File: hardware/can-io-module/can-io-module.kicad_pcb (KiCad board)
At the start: 2 copper layers, 96 x 86 mm, 79 parts, among them J1 ECU_FCI_24P_RightAngle, Q1 60V P-channel reverse polarity, Q4 60V logic N-MOS RELAY1, Q5 60V logic N-MOS RELAY2, U1 STM32G0B1CBT6, U10 MAX31855KASA+, U11 Schmitt Flex front end, U2 LMR16006Y-Q1, U3 3V3 LDO 300mA, U4 SENSOR_5V load switch, U5 74HCT4051 1K excitation, U6 74HCT4051 4K7 excitation, U7 L9613, U8 TJA1051T/3, U9 TLV9002-Q1

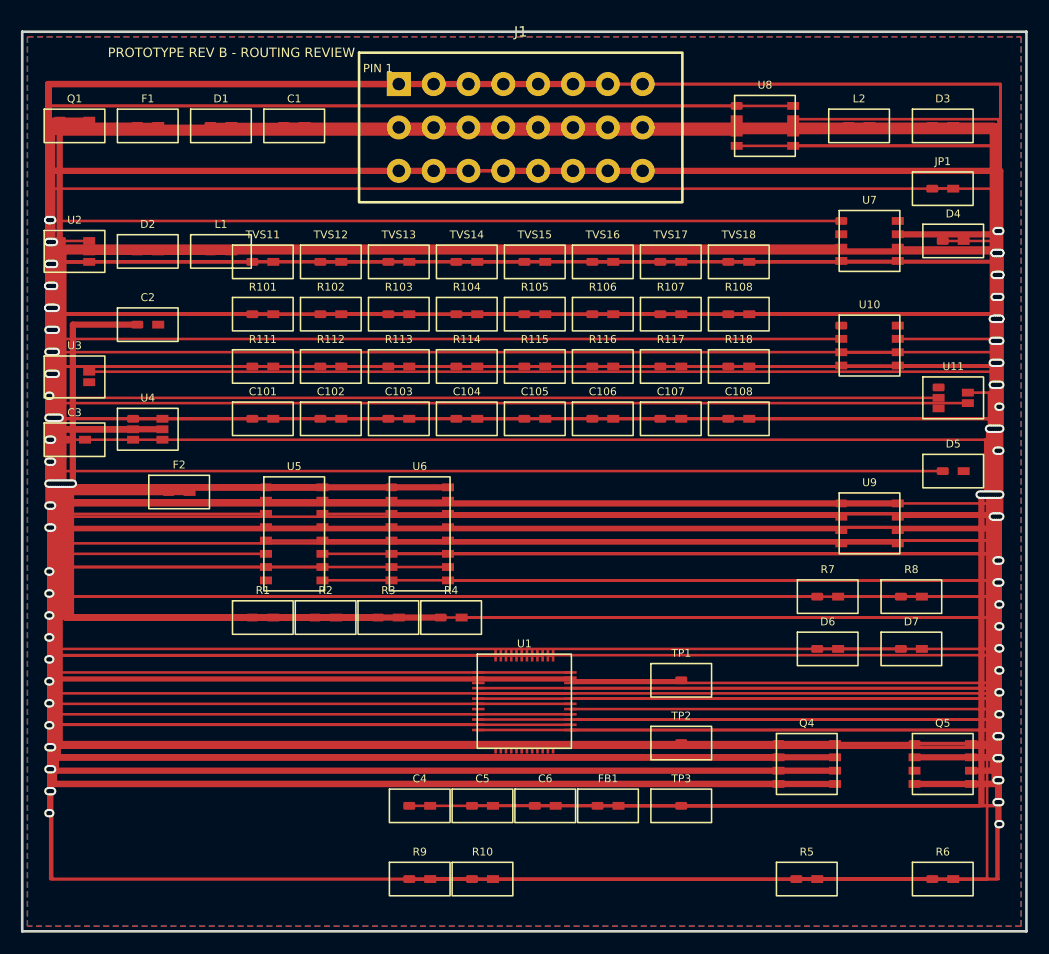
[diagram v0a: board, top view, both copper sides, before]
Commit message: feat: check in verified two-layer CAN IO route
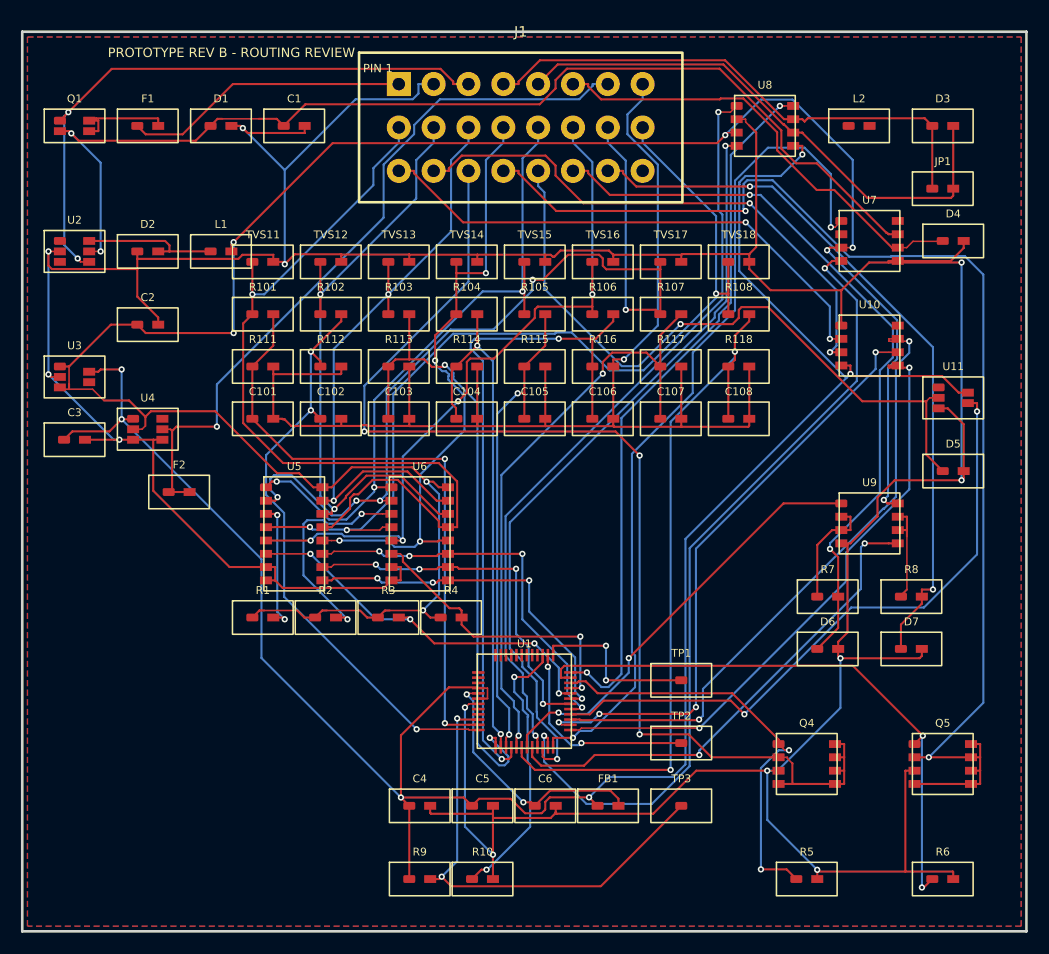
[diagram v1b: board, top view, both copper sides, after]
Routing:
- net +3V3: track 843.1 -> 209.9 mm, vias 12 -> 6
- net RELAY_OUT1: track 704.0 -> 113.5 mm, vias 7 -> 3
- net POWER_GND: track 0.00 -> 415.8 mm, vias 0 -> 12
- net +5V: track 610.4 -> 216.9 mm, vias 14 -> 8
- net VBAT_PROTECTED: track 494.7 -> 105.5 mm, vias 5 -> 2
- net AOUT1_OP: track 319.1 -> 10.9 mm, vias 3 -> 0
- net AIN2: track 363.2 -> 61.8 mm, vias 5 -> 2
- net CAN_L: track 341.2 -> 52.5 mm, vias 4 -> 0
- net AIN4: track 337.8 -> 60.7 mm, vias 5 -> 4
- net ADC_IN2: track 321.1 -> 57.6 mm, vias 4 -> 3
- net AIN6: track 318.0 -> 70.7 mm, vias 5 -> 4
- net ADC_IN4: track 273.1 -> 50.5 mm, vias 4 -> 2
- net ADC_IN7: track 281.1 -> 58.9 mm, vias 4 -> 2
- net AOUT2: track 277.1 -> 68.9 mm, vias 3 -> 2
- net ADC_IN5: track 249.4 -> 46.7 mm, vias 4 -> 2
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
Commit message: feat: generate connected CAN IO schematic and SWD header
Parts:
- added J2: SWD_1x05_P2.54mm_DNP, Connector_PinHeader_2.54mm:PinHeader_1x05_P2.54mm_Vertical, F.Cu at (86.0, 92.0)
- U4: footprint DIY_DASH:SC70-6 -> DIY_DASH:SC70-5
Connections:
- F2 pad 1: SENSOR_5V -> SENSOR_5V_SW
- L2 pad 1: (no net) -> CAN_H_PROTECTED
- L2 pad 2: (no net) -> CAN_L_PROTECTED
- U1 pad 15: ADC_IN5 -> DAC1_RAW
- U1 pad 16: ADC_IN6 -> DAC2_RAW
- U1 pad 17: ADC_IN7 -> ADC_IN5
- U1 pad 18: ADC_IN8 -> ADC_IN6
- U1 pad 19: DAC1_RAW -> ADC_IN7
- U1 pad 20: DAC2_RAW -> ADC_IN8
- U1 pad 21: CAN_TX -> BOOT0
- U1 pad 22: CAN_RX -> VBAT_MON
- U1 pad 23: KTX -> V5_MON
- U1 pad 24: KRX -> V3V3_MON
- U1 pad 25: EGT_SCK -> RELAY2_GATE
- U1 pad 26: EGT_CS -> CAN_SILENT
- U1 pad 27: EGT_SO -> SENSOR_5V_EN
- U1 pad 29: PULL_A0 -> IGN_SENSE
- U1 pad 30: PULL_A1 -> PULL_4K7_EN_N
- U1 pad 31: PULL_A2 -> RELAY1_GATE
- U1 pad 32: PULL_1K_EN_N -> SERVICE
- U1 pad 33: PULL_4K7_EN_N -> CAN_RX
- U1 pad 34: RELAY1_GATE -> CAN_TX
- U1 pad 35: RELAY2_GATE -> SWDIO
- U1 pad 36: CAN_SILENT -> SWCLK
- U1 pad 37: SWDIO -> KLINE_ENABLE
- U1 pad 38: SWCLK -> PULL_A0
- U1 pad 39: BOOT0 -> PULL_A1
- U1 pad 40: (no net) -> PULL_A2
- U1 pad 41: (no net) -> PULL_1K_EN_N
- U1 pad 42: (no net) -> EGT_SCK
- U1 pad 43: (no net) -> EGT_SO
- U1 pad 44: (no net) -> EGT_CS
- U1 pad 45: (no net) -> KTX
- U1 pad 46: (no net) -> KRX
- U4 pad 1: +3V3 -> SENSOR_5V_SW
- U4 pad 2: +5V -> POWER_GND
- U4 pad 3: POWER_GND -> SENSOR_5V_OC
- U4 pad 4: POWER_GND -> SENSOR_5V_EN
- U4 pad 5: SENSOR_5V -> +5V
- U8 pad 6: CAN_L -> CAN_L_PROTECTED
- U8 pad 7: CAN_H -> CAN_H_PROTECTED
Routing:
- net +3V3: track 209.9 -> 808.2 mm, vias 6 -> 12
- net RELAY_OUT1: track 113.5 -> 704.0 mm, vias 3 -> 7
- net POWER_GND: track 415.8 -> 0.00 mm, vias 12 -> 0
- net +5V: track 216.9 -> 613.7 mm, vias 8 -> 14
- net VBAT_PROTECTED: track 105.5 -> 494.7 mm, vias 2 -> 5
- net AOUT1_OP: track 10.9 -> 319.1 mm, vias 0 -> 3
- net AIN2: track 61.8 -> 363.2 mm, vias 2 -> 5
- net CAN_L: track 52.5 -> 350.0 mm, vias 0 -> 4
- net AIN4: track 60.7 -> 337.8 mm, vias 4 -> 5
- net AIN6: track 70.7 -> 318.0 mm, vias 4 -> 5
- net ADC_IN2: track 57.6 -> 288.4 mm, vias 3 -> 4
- net NRST: track 45.5 -> 260.6 mm, vias 2 -> 4
- net ADC_IN7: track 58.9 -> 269.7 mm, vias 2 -> 4
- net AOUT2: track 68.9 -> 277.1 mm, vias 2 -> 3
- net AIN7: track 87.6 -> 288.3 mm
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
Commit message: fix: make CAN IO symbol and footprint libraries self contained
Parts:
- J2: footprint Connector_PinHeader_2.54mm:PinHeader_1x05_P2.54mm_Vertical -> DIY_DASH:SWD_1x05_P2.54mm_Vertical
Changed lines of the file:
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@@
     (pad "24" thru_hole oval (at 23.31 8.30) (size 2.3 2.3) (drill 1.2) (layers "*.Cu" "*.Mask") (net 24 "SERVICE") (pinfunction "SERVICE") (pintype "passive"))
   )
-  (footprint "Connector_PinHeader_2.54mm:PinHeader_1x05_P2.54mm_Vertical" (layer "F.Cu")
+  (footprint "DIY_DASH:SWD_1x05_P2.54mm_Vertical" (layer "F.Cu")
     (at 86.0 92.0)
     (property "Reference" "J2" (at 0 -2.33) (layer "F.SilkS") (effects (font (size 0.8 0.8) (thickness 0.12))))

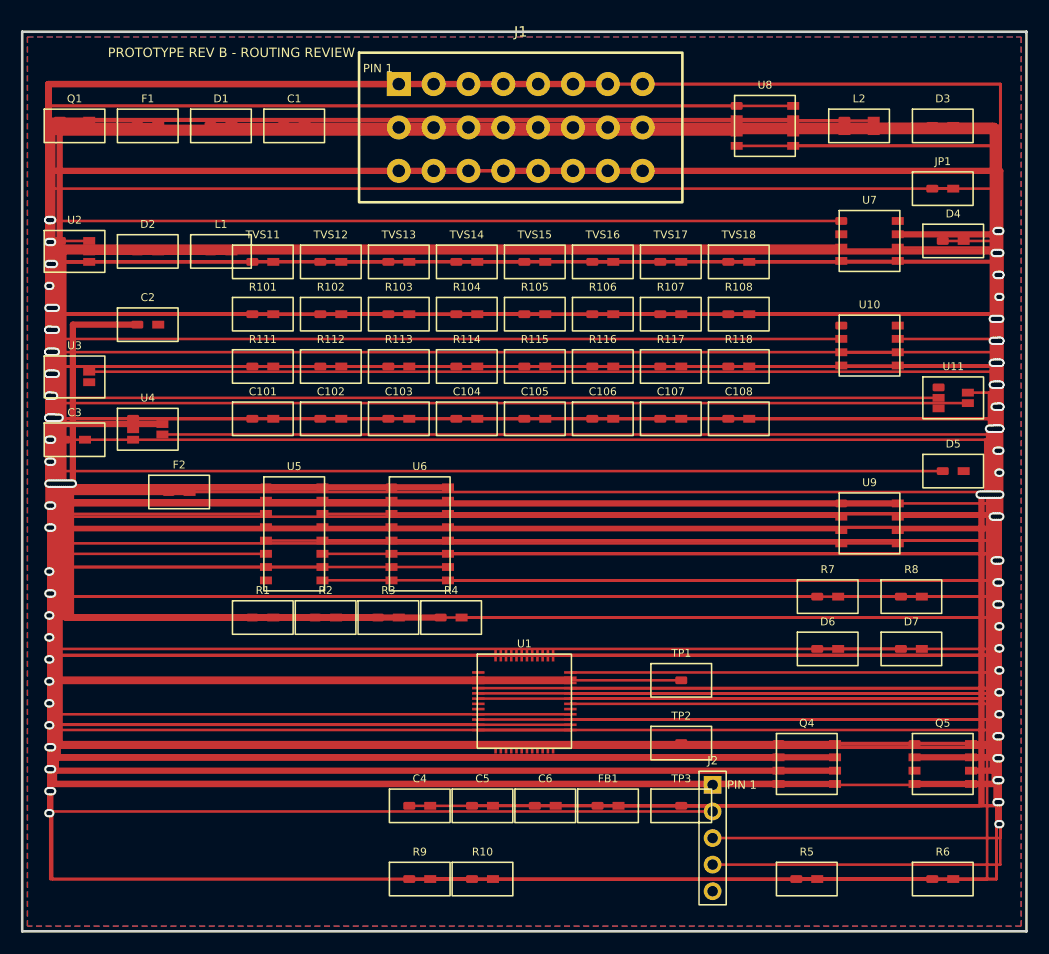
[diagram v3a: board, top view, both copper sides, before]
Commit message: fix: complete CAN IO power monitor support circuits
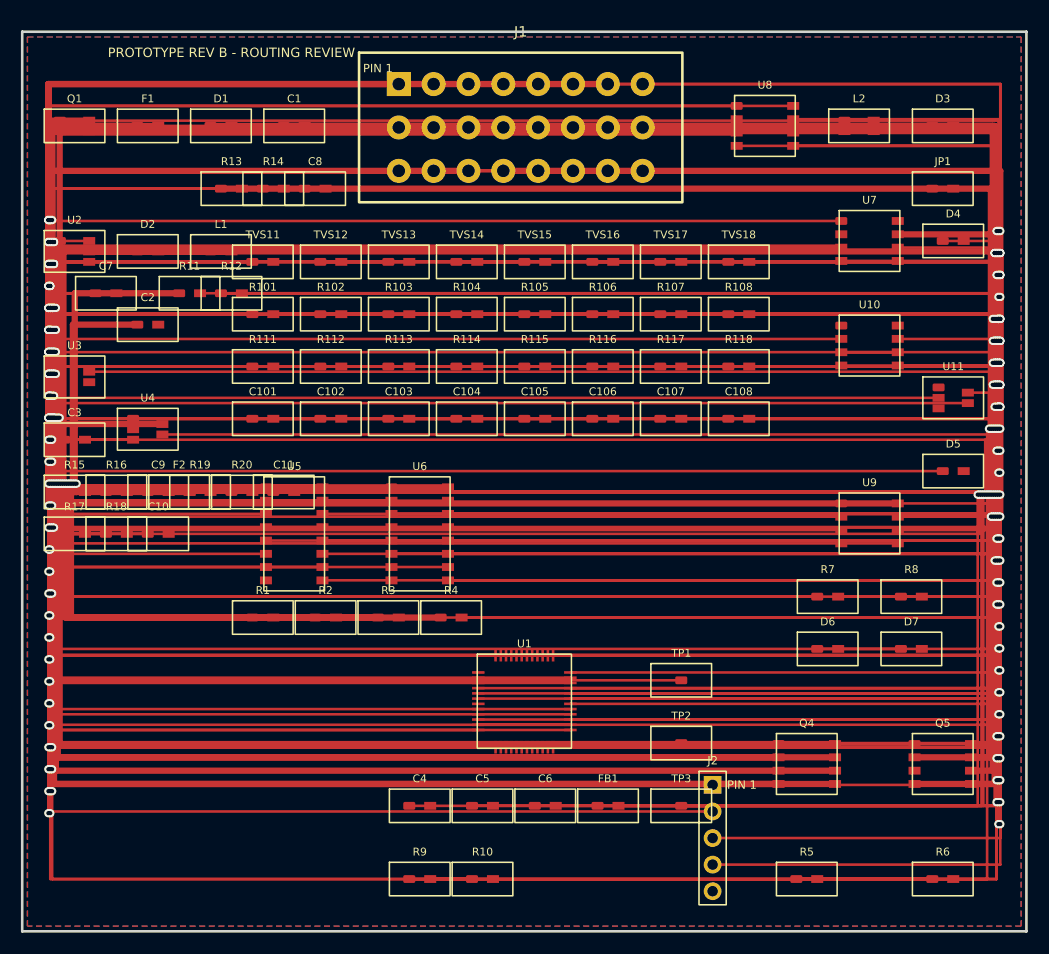
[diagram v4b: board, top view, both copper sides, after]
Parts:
- added C10: 10nF 3V3 monitor filter, DIY_DASH:0603, F.Cu at (33.0, 68.0)
- added C11: 10nF IGN sense filter, DIY_DASH:0603, F.Cu at (45.0, 64.0)
- added C7: 100nF buck bootstrap, DIY_DASH:0603, F.Cu at (28.0, 45.0)
- added C8: 10nF VBAT monitor filter, DIY_DASH:0603, F.Cu at (48.0, 35.0)
- added C9: 10nF 5V monitor filter, DIY_DASH:0603, F.Cu at (33.0, 64.0)
- added R11: 40.2k 1% buck FB upper, DIY_DASH:0603, F.Cu at (36.0, 45.0)
- added R12: 10.0k 1% buck FB lower, DIY_DASH:0603, F.Cu at (40.0, 45.0)
- added R13: 100k 1% VBAT monitor upper, DIY_DASH:0603, F.Cu at (40.0, 35.0)
- added R14: 15.0k 1% VBAT monitor lower, DIY_DASH:0603, F.Cu at (44.0, 35.0)
- added R15: 10.0k 1% 5V monitor upper, DIY_DASH:0603, F.Cu at (25.0, 64.0)
- added R16: 18.0k 1% 5V monitor lower, DIY_DASH:0603, F.Cu at (29.0, 64.0)
- added R17: 1.00k 1% 3V3 monitor upper, DIY_DASH:0603, F.Cu at (25.0, 68.0)
- added R18: 100k 1% 3V3 monitor lower, DIY_DASH:0603, F.Cu at (29.0, 68.0)
- added R19: 100k 1% IGN sense upper, DIY_DASH:0603, F.Cu at (37.0, 64.0)
- added R20: 15.0k 1% IGN sense lower, DIY_DASH:0603, F.Cu at (41.0, 64.0)
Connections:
- U1 pad 37: KLINE_ENABLE -> (no net)
- U1 pad 47: (no net) -> SENSOR_5V_OC
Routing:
- net V5_MON: track 0.00 -> 413.6 mm, vias 0 -> 4
- net BUCK_FB: track 0.00 -> 314.2 mm, vias 0 -> 3
- net IGN_SENSE: track 0.00 -> 195.6 mm, vias 0 -> 4
- net V3V3_MON: track 0.00 -> 190.3 mm, vias 0 -> 4
- net VBAT_MON: track 0.00 -> 174.4 mm, vias 0 -> 4
- net ADC_IN1: track 148.6 -> 311.5 mm
- net ADC_IN8: track 169.0 -> 289.7 mm
- net ADC_IN2: track 288.4 -> 168.7 mm
- net CAN_H_PROTECTED: track 187.4 -> 72.7 mm
- net CAN_L_PROTECTED: track 74.7 -> 185.2 mm
- net VBAT_PROTECTED: track 494.7 -> 600.5 mm, vias 5 -> 6
- net SENSOR_5V_OC: track 0.00 -> 101.3 mm, vias 0 -> 2
- net +3V3: track 808.2 -> 901.4 mm, vias 12 -> 13
- net ADC_IN7: track 269.7 -> 187.2 mm
- net ADC_IN3: track 188.6 -> 268.9 mm
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
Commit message: fix: separate CAN IO power monitor footprints
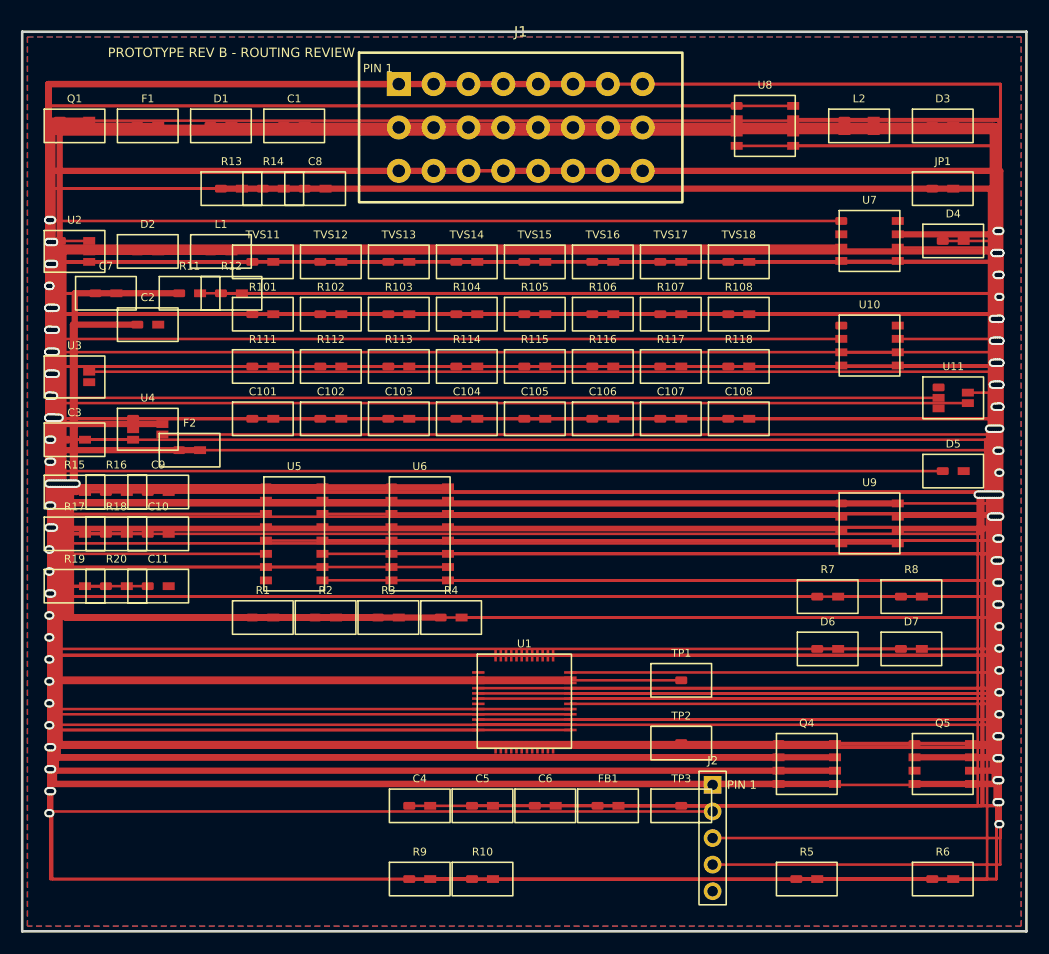
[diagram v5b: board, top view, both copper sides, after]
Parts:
- moved C11 15.0 mm to (33.0, 73.0)
- moved R19 15.0 mm to (25.0, 73.0)
- moved R20 15.0 mm to (29.0, 73.0)
- moved F2 4.12 mm to (36.0, 60.0)
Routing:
- net IGN_SENSE: track 195.6 -> 186.6 mm
- net SENSOR_5V_SW: track 192.7 -> 187.7 mm
- net SENSOR_5V: track 106.0 -> 103.0 mm
- net IGN: track 111.2 -> 108.2 mm
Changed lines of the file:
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@@
   )
   (footprint "DIY_DASH:0603" (layer "F.Cu")
-    (at 45.00 64.00)
+    (at 33.00 73.00)
     (property "Reference" "C11" (at 0 -2.60) (layer "F.SilkS") (effects (font (size 0.75 0.75) (thickness 0.12))))
     (property "Value" "10nF IGN sense filter" (at 0 2.60) (layer "F.Fab") (effects (font (size 0.6 0.6) (thickness 0.10))))
@@
   )
   (footprint "DIY_DASH:0603" (layer "F.Cu")
-    (at 37.00 64.00)
+    (at 25.00 73.00)
     (property "Reference" "R19" (at 0 -2.60) (layer "F.SilkS") (effects (font (size 0.75 0.75) (thickness 0.12))))
     (property "Value" "100k 1% IGN sense upper" (at 0 2.60) (layer "F.Fab") (effects (font (size 0.6 0.6) (thickness 0.10))))
@@
   )
   (footprint "DIY_DASH:0603" (layer "F.Cu")
-    (at 41.00 64.00)
+    (at 29.00 73.00)
     (property "Reference" "R20" (at 0 -2.60) (layer "F.SilkS") (effects (font (size 0.75 0.75) (thickness 0.12))))
     (property "Value" "15.0k 1% IGN sense lower" (at 0 2.60) (layer "F.Fab") (effects (font (size 0.6 0.6) (thickness 0.10))))
@@
   )
   (footprint "DIY_DASH:1206" (layer "F.Cu")
-    (at 35.00 64.00)
+    (at 36.00 60.00)
     (property "Reference" "F2" (at 0 -2.60) (layer "F.SilkS") (effects (font (size 0.75 0.75) (thickness 0.12))))
     (property "Value" "250mA resettable sensor fuse" (at 0 2.60) (layer "F.Fab") (effects (font (size 0.6 0.6) (thickness 0.10))))
@@
   (segment (start 22.86 28.50) (end 22.86 40.10) (width 0.25) (layer "F.Cu") (net 3))
   (segment (start 22.50 40.10) (end 22.86 40.10) (width 0.25) (layer "B.Cu") (net 3))
-  (segment (start 36.00 64.00) (end 23.04 64.00) (width 0.25) (layer "F.Cu") (net 3))
-  (segment (start 23.04 64.00) (end 23.04 40.10) (width 0.25) (layer "F.Cu") (net 3))
+  (segment (start 24.00 73.00) (end 23.04 73.00) (width 0.25) (layer "F.Cu") (net 3))
+  (segment (start 23.04 73.00) (end 23.04 40.10) (width 0.25) (layer "F.Cu") (net 3))
   (segment (start 22.50 40.10) (end 23.04 40.10) (width 0.25) (layer "B.Cu") (net 3))
   (segment (start 65.99 25.00) (end 113.50 25.00) (width 0.25) (layer "F.Cu") (net 4))
@@
   (segment (start 75.98 25.00) (end 22.50 25.00) (width 0.6) (layer "F.Cu") (net 7))
   (segment (start 22.50 25.00) (end 22.50 44.30) (width 0.6) (layer "F.Cu") (net 7))
-  (segment (start 36.00 64.00) (end 22.68 64.00) (width 0.6) (layer "F.Cu") (net 7))
-  (segment (start 22.68 64.00) (end 22.68 44.30) (width 0.6) (layer "F.Cu") (net 7))
+  (segment (start 37.00 60.00) (end 22.68 60.00) (width 0.6) (layer "F.Cu") (net 7))
+  (segment (start 22.68 60.00) (end 22.68 44.30) (width 0.6) (layer "F.Cu") (net 7))
   (segment (start 22.50 44.30) (end 22.68 44.30) (width 0.6) (layer "B.Cu") (net 7))
   (segment (start 56.00 29.15) (end 22.50 29.15) (width 0.25) (layer "F.Cu") (net 9))
@@
   (segment (start 30.60 57.00) (end 113.50 57.00) (width 0.25) (layer "F.Cu") (net 64))
   (segment (start 113.50 57.00) (end 113.50 45.35) (width 0.25) (layer "F.Cu") (net 64))
-  (segment (start 34.00 64.00) (end 113.32 64.00) (width 0.25) (layer "F.Cu") (net 64))
-  (segment (start 113.32 64.00) (end 113.32 45.35) (width 0.25) (layer "F.Cu") (net 64))
+  (segment (start 35.00 60.00) (end 113.32 60.00) (width 0.25) (layer "F.Cu") (net 64))
+  (segment (start 113.32 60.00) (end 113.32 45.35) (width 0.25) (layer "F.Cu") (net 64))
   (segment (start 113.50 45.35) (end 113.32 45.35) (width 0.25) (layer "B.Cu") (net 64))
   (segment (start 72.40 84.75) (end 22.50 84.75) (width 0.25) (layer "F.Cu") (net 65))
   (segment (start 22.50 84.75) (end 22.50 46.40) (width 0.25) (layer "F.Cu") (net 65))
-  (segment (start 44.00 64.00) (end 22.68 64.00) (width 0.25) (layer "F.Cu") (net 65))
-  (segment (start 22.68 64.00) (end 22.68 46.40) (width 0.25) (layer "F.Cu") (net 65))
+  (segment (start 32.00 73.00) (end 22.68 73.00) (width 0.25) (layer "F.Cu") (net 65))
+  (segment (start 22.68 73.00) (end 22.68 46.40) (width 0.25) (layer "F.Cu") (net 65))
   (segment (start 22.50 46.40) (end 22.68 46.40) (width 0.25) (layer "B.Cu") (net 65))
-  (segment (start 38.00 64.00) (end 22.86 64.00) (width 0.25) (layer "F.Cu") (net 65))
-  (segment (start 22.86 64.00) (end 22.86 46.40) (width 0.25) (layer "F.Cu") (net 65))
+  (segment (start 26.00 73.00) (end 22.86 73.00) (width 0.25) (layer "F.Cu") (net 65))
+  (segment (start 22.86 73.00) (end 22.86 46.40) (width 0.25) (layer "F.Cu") (net 65))
   (segment (start 22.50 46.40) (end 22.86 46.40) (width 0.25) (layer "B.Cu") (net 65))
-  (segment (start 40.00 64.00) (end 23.04 64.00) (width 0.25) (layer "F.Cu") (net 65))
-  (segment (start 23.04 64.00) (end 23.04 46.40) (width 0.25) (layer "F.Cu") (net 65))
+  (segment (start 28.00 73.00) (end 23.04 73.00) (width 0.25) (layer "F.Cu") (net 65))
+  (segment (start 23.04 73.00) (end 23.04 46.40) (width 0.25) (layer "F.Cu") (net 65))
   (segment (start 22.50 46.40) (end 23.04 46.40) (width 0.25) (layer "B.Cu") (net 65))
   (segment (start 93.70 28.36) (end 113.50 28.36) (width 0.25) (layer "F.Cu") (net 66))

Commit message: chore: store verified CAN IO route [skip ci]
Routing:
- net +3V3: track 901.4 -> 225.2 mm, vias 13 -> 5
- net RELAY_OUT1: track 704.0 -> 99.5 mm, vias 7 -> 2
- net VBAT_PROTECTED: track 600.5 -> 108.4 mm, vias 6 -> 2
- net POWER_GND: track 0.00 -> 473.2 mm, vias 0 -> 11
- net +5V: track 649.1 -> 209.8 mm, vias 16 -> 5
- net V5_MON: track 413.6 -> 57.8 mm, vias 4 -> 2
- net AOUT1_OP: track 319.1 -> 11.1 mm, vias 3 -> 0
- net AIN2: track 363.2 -> 62.3 mm, vias 5 -> 2
- net CAN_L: track 350.0 -> 49.2 mm, vias 4 -> 0
- net BUCK_FB: track 314.2 -> 19.4 mm, vias 3 -> 0
- net AIN4: track 337.8 -> 66.3 mm, vias 5 -> 4
- net ADC_IN1: track 311.5 -> 58.9 mm, vias 4 -> 2
- net AIN6: track 318.0 -> 69.1 mm, vias 5 -> 3
- net ADC_IN8: track 289.7 -> 51.9 mm, vias 4 -> 2
- net AIN7: track 288.3 -> 74.2 mm, vias 5 -> 4
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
